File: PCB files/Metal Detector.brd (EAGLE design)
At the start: 100 x 80 mm, 121 parts, among them IC1 NE5534AD, IC2 BQ24133RGYR, IC3 LM317MBSTT3, IC4 ESP32-WROOM-32UE-N4, IC5 CP2102, IC6 LM317MBSTT3, J1 L-KLS1-TSJ3.5-013, J2/BATTERY DG128-5.0-02P-14, Q1 IRF740, Q2 BC556, Q3 SI2312CDS-T1-GE3, Q4 MBT3904DW1T1, Q5 SI2312CDS-T1-GE3, Q6 SI2323CDS-T1-GE3, T1 BC547, X1 A1944-50, X2 DC21MMX

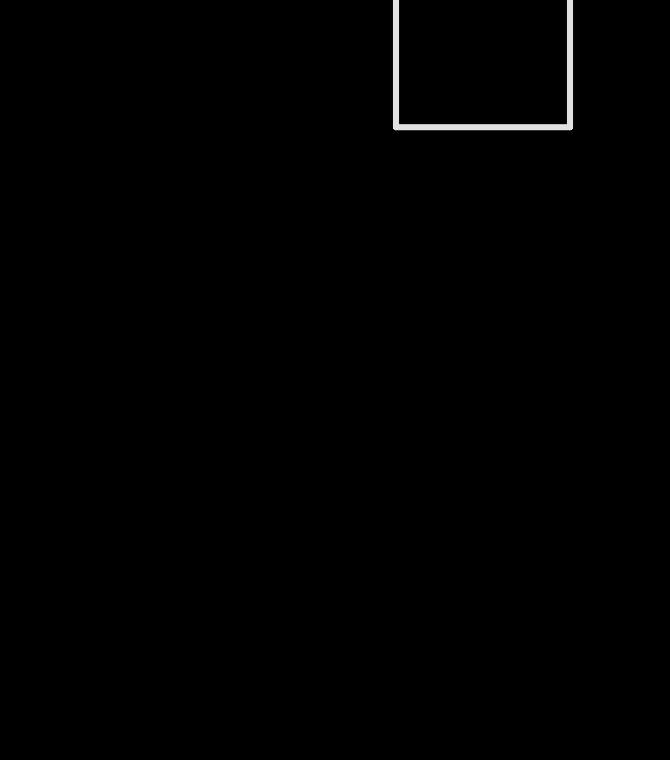
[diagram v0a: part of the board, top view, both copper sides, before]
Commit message: Add files via upload
adding speaker's control circuit (Design process still in progress)
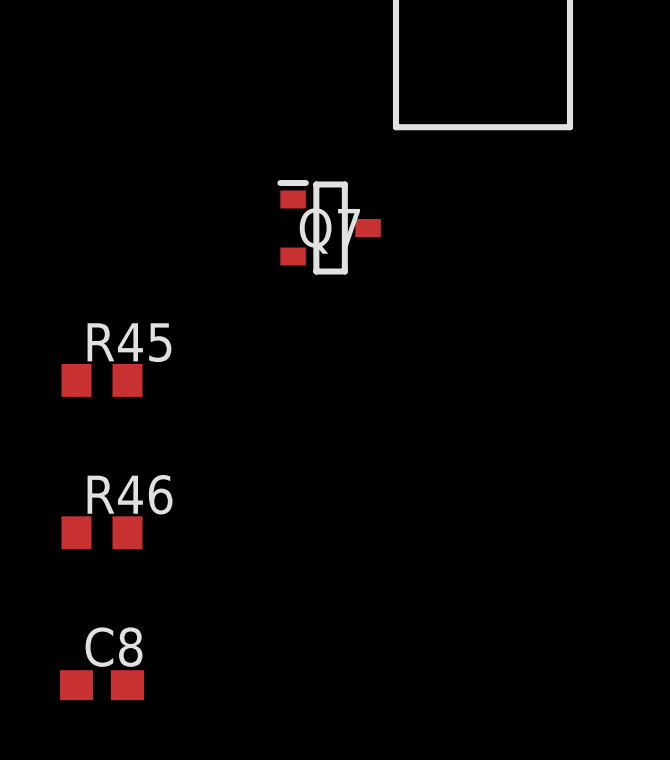
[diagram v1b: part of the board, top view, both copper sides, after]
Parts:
- added C8: 100nF, rcl:C0603
- added Q7: BC847AE6327HTSA1, BC847AE6327HTSA1:SOT95P240X110-3N
- added R45: 1KΩ, rcl:R0603
- added R46: 150Ω, rcl:R0603
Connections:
- new net N$26: LS1.2, Q7.3
- new net N$29: Q7.1, R45.1
- new net N$30: C8.2, LS1.1, R46.2
- new net N$31: R45.2
- net GND: now also Q7.2
- net VCC: now also C8.1, R46.1
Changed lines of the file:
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@@
 <attribute name="VALUE" x="-145.04" y="-559.55" size="1.27" layer="27" rot="R90"/>
+</element>
+<element name="Q7" library="BC847AE6327HTSA1" package="SOT95P240X110-3N" value="BC847AE6327HTSA1" x="-160.02" y="-608.33" smashed="yes">
+<attribute name="ARROW_PART_NUMBER" value="BC847AE6327HTSA1" x="-160.02" y="-608.33" size="1.778" layer="27" display="off"/>
+<attribute name="ARROW_PRICE-STOCK" value="https://www.arrow.com/en/products/bc847ae6327htsa1/infineon-technologies-ag?region=nac" x="-160.02" y="-608.33" size="1.778" layer="27" display="off"/>
+<attribute name="DESCRIPTION" value="TRANS NPN 45V 0.1A SOT-23" x="-160.02" y="-608.33" size="1.778" layer="27" display="off"/>
+<attribute name="HEIGHT" value="1.1mm" x="-160.02" y="-608.33" size="1.778" layer="27" display="off"/>
+<attribute name="MANUFACTURER_NAME" value="Infineon" x="-160.02" y="-608.33" size="1.778" layer="27" display="off"/>
+<attribute name="MANUFACTURER_PART_NUMBER" value="BC847AE6327HTSA1" x="-160.02" y="-608.33" size="1.778" layer="27" display="off"/>
+<attribute name="MOUSER_PART_NUMBER" value="726-BC847AE6327HTSA1" x="-160.02" y="-608.33" size="1.778" layer="27" display="off"/>
+<attribute name="MOUSER_PRICE-STOCK" value="https://www.mouser.co.uk/ProductDetail/Infineon-Technologies/BC847AE6327HTSA1?qs=K00xGehIljsR0IXot1V2vQ%3D%3D" x="-160.02" y="-608.33" size="1.778" layer="27" display="off"/>
+<attribute name="NAME" x="-160.02" y="-608.33" size="1.27" layer="25" align="center"/>
+<attribute name="VALUE" x="-160.02" y="-608.33" size="1.27" layer="27" align="center"/>
+</element>
+<element name="R45" library="rcl" library_urn="urn:adsk.eagle:library:334" package="R0603" package3d_urn="urn:adsk.eagle:package:23555/3" value="1KΩ" x="-167.64" y="-613.41" smashed="yes">
+<attribute name="NAME" x="-168.275" y="-612.775" size="1.27" layer="25"/>
+<attribute name="POPULARITY" value="70" x="-167.64" y="-613.41" size="1.778" layer="27" display="off"/>
+<attribute name="SPICEPREFIX" value="R" x="-167.64" y="-613.41" size="1.778" layer="27" display="off"/>
+<attribute name="VALUE" x="-168.275" y="-615.315" size="1.27" layer="27"/>
+</element>
+<element name="R46" library="rcl" library_urn="urn:adsk.eagle:library:334" package="R0603" package3d_urn="urn:adsk.eagle:package:23555/3" value="150Ω" x="-167.64" y="-618.49" smashed="yes">
+<attribute name="NAME" x="-168.275" y="-617.855" size="1.27" layer="25"/>
+<attribute name="POPULARITY" value="70" x="-167.64" y="-618.49" size="1.778" layer="27" display="off"/>
+<attribute name="SPICEPREFIX" value="R" x="-167.64" y="-618.49" size="1.778" layer="27" display="off"/>
+<attribute name="VALUE" x="-168.275" y="-620.395" size="1.27" layer="27"/>
+</element>
+<element name="C8" library="rcl" library_urn="urn:adsk.eagle:library:334" package="C0603" package3d_urn="urn:adsk.eagle:package:23616/2" value="100nF" x="-167.64" y="-623.57" smashed="yes">
+<attribute name="NAME" x="-168.275" y="-622.935" size="1.27" layer="25"/>
+<attribute name="POPULARITY" value="73" x="-167.64" y="-623.57" size="1.778" layer="27" display="off"/>
+<attribute name="SPICEPREFIX" value="C" x="-167.64" y="-623.57" size="1.778" layer="27" display="off"/>
+<attribute name="VALUE" x="-168.275" y="-625.475" size="1.27" layer="27"/>
 </element>
 </elements>
@@
 <contactref element="DS1" pad="2"/>
 <contactref element="R44" pad="1E"/>
+<contactref element="Q7" pad="2"/>
 <wire x1="-119.06" y1="-351.79" x2="-125.31" y2="-381" width="0" layer="19" extent="1-1"/>
 <wire x1="-123.9" y1="-335.28" x2="-119.06" y2="-351.79" width="0" layer="19" extent="1-1"/>
@@
 <wire x1="-141.39" y1="-598.17" x2="-138.43" y2="-593.09" width="0" layer="19" extent="1-1"/>
 <wire x1="-141.39" y1="-603.25" x2="-141.39" y2="-598.17" width="0" layer="19" extent="1-1"/>
+<wire x1="-161.27" y1="-609.28" x2="-141.39" y2="-603.25" width="0" layer="19" extent="1-1"/>
 <wire x1="-62.23" y1="-153.67" x2="-119.25" y2="-259.08" width="0" layer="19" extent="1-1"/>
 <wire x1="-16.51" y1="-153.67" x2="-62.23" y2="-153.67" width="0" layer="19" extent="1-1"/>
@@
 <contactref element="DS1" pad="19"/>
 <contactref element="R44" pad="1A"/>
+<contactref element="R46" pad="1"/>
+<contactref element="C8" pad="1"/>
 <wire x1="-143.09" y1="-598.17" x2="-143.09" y2="-603.25" width="0" layer="19" extent="1-1"/>
 <wire x1="-143.09" y1="-585.47" x2="-143.09" y2="-598.17" width="0" layer="19" extent="1-1"/>
+<wire x1="-168.49" y1="-618.49" x2="-143.09" y2="-603.25" width="0" layer="19" extent="1-1"/>
+<wire x1="-168.49" y1="-623.57" x2="-168.49" y2="-618.49" width="0" layer="19" extent="1-1"/>
 <wire x1="-159.94" y1="-553.57" x2="-143.09" y2="-585.47" width="0" layer="19" extent="1-1"/>
 <wire x1="-141.82" y1="-544.83" x2="-159.94" y2="-553.57" width="0" layer="19" extent="1-1"/>
@@
 <wire x1="-154.94" y1="-553.57" x2="-59.69" y2="-153.67" width="0" layer="19" extent="1-1"/>
 </signal>
+<signal name="N$26">
+<contactref element="LS1" pad="2"/>
+<contactref element="Q7" pad="3"/>
+<wire x1="-158.77" y1="-608.33" x2="-111.84" y2="-165.1" width="0" layer="19" extent="1-1"/>
+</signal>
+<signal name="N$29">
+<contactref element="R45" pad="1"/>
+<contactref element="Q7" pad="1"/>
+<wire x1="-161.27" y1="-607.38" x2="-168.49" y2="-613.41" width="0" layer="19" extent="1-1"/>
+</signal>
+<signal name="N$30">
+<contactref element="R46" pad="2"/>
+<contactref element="LS1" pad="1"/>
+<contactref element="C8" pad="2"/>
+<wire x1="-166.79" y1="-618.49" x2="-116.84" y2="-165.1" width="0" layer="19" extent="1-1"/>
+<wire x1="-166.79" y1="-623.57" x2="-166.79" y2="-618.49" width="0" layer="19" extent="1-1"/>
+</signal>
+<signal name="N$31">
+<contactref element="R45" pad="2"/>
+</signal>
 </signals>

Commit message: Add files via upload
Connected and added Spekers, volume and sensitivty connections with MCU
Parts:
- R45: value 1KΩ -> 1kΩ
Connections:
- net GND: now also R11.1E
- net IO32: now also R45.2
- net IO34: now also R12.1S
- net IO35: now also R11.1S
- net N$30: now also R12.1A; no longer LS1.1
- net N$31: now also LS1.1, R12.1E; no longer R45.2
- net VCC: now also R11.1A
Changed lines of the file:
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@@
 <attribute name="VALUE" x="-160.02" y="-608.33" size="1.27" layer="27" align="center"/>
 </element>
-<element name="R45" library="rcl" library_urn="urn:adsk.eagle:library:334" package="R0603" package3d_urn="urn:adsk.eagle:package:23555/3" value="1KΩ" x="-167.64" y="-613.41" smashed="yes">
+<element name="R45" library="rcl" library_urn="urn:adsk.eagle:library:334" package="R0603" package3d_urn="urn:adsk.eagle:package:23555/3" value="1kΩ" x="-167.64" y="-613.41" smashed="yes">
 <attribute name="NAME" x="-168.275" y="-612.775" size="1.27" layer="25"/>
 <attribute name="POPULARITY" value="70" x="-167.64" y="-613.41" size="1.778" layer="27" display="off"/>
@@
 <contactref element="R44" pad="1E"/>
 <contactref element="Q7" pad="2"/>
+<contactref element="R11" pad="1E"/>
 <wire x1="-119.06" y1="-351.79" x2="-125.31" y2="-381" width="0" layer="19" extent="1-1"/>
 <wire x1="-123.9" y1="-335.28" x2="-119.06" y2="-351.79" width="0" layer="19" extent="1-1"/>
@@
 <wire x1="-62.23" y1="-153.67" x2="-119.25" y2="-259.08" width="0" layer="19" extent="1-1"/>
 <wire x1="-16.51" y1="-153.67" x2="-62.23" y2="-153.67" width="0" layer="19" extent="1-1"/>
-<wire x1="-73.66" y1="-79.5528" x2="-62.23" y2="-153.67" width="0" layer="19" extent="1-1"/>
+<wire x1="-85.17" y1="-105.26" x2="-62.23" y2="-153.67" width="0" layer="19" extent="1-1"/>
+<wire x1="-73.66" y1="-79.5528" x2="-85.17" y2="-105.26" width="0" layer="19" extent="1-1"/>
 <wire x1="-68.6562" y1="-76.5556" x2="-73.66" y2="-79.5528" width="0" layer="19" extent="1-1"/>
 <wire x1="-69.85" y1="-64.77" x2="-68.6562" y2="-76.5556" width="0" layer="19" extent="1-1"/>
@@
 <contactref element="R46" pad="1"/>
 <contactref element="C8" pad="1"/>
+<contactref element="R11" pad="1A"/>
 <wire x1="-143.09" y1="-598.17" x2="-143.09" y2="-603.25" width="0" layer="19" extent="1-1"/>
 <wire x1="-143.09" y1="-585.47" x2="-143.09" y2="-598.17" width="0" layer="19" extent="1-1"/>
@@
 <wire x1="-64.77" y1="-153.67" x2="-116.13" y2="-274.32" width="0" layer="19" extent="1-1"/>
 <wire x1="-19.05" y1="-153.67" x2="-64.77" y2="-153.67" width="0" layer="19" extent="1-1"/>
-<wire x1="-67.125" y1="-65.52" x2="-64.77" y2="-153.67" width="0" layer="19" extent="1-1"/>
+<wire x1="-95.17" y1="-105.26" x2="-64.77" y2="-153.67" width="0" layer="19" extent="1-1"/>
+<wire x1="-67.125" y1="-65.52" x2="-95.17" y2="-105.26" width="0" layer="19" extent="1-1"/>
 <wire x1="-64.64" y1="-55.88" x2="-67.125" y2="-65.52" width="0" layer="19" extent="1-1"/>
 <wire x1="-63.92" y1="-50.8" x2="-64.64" y2="-55.88" width="0" layer="19" extent="1-1"/>
@@
 <signal name="IO34">
 <contactref element="IC4" pad="6"/>
+<contactref element="R12" pad="1S"/>
+<wire x1="-72.25" y1="-19.53" x2="-111.76" y2="-105.26" width="0" layer="19" extent="1-1"/>
 </signal>
 <signal name="IO35">
 <contactref element="IC4" pad="7"/>
+<contactref element="R11" pad="1S"/>
+<wire x1="-72.25" y1="-20.8" x2="-90.17" y2="-105.26" width="0" layer="19" extent="1-1"/>
 </signal>
 <signal name="IO32">
 <contactref element="IC4" pad="8"/>
+<contactref element="R45" pad="2"/>
+<wire x1="-166.79" y1="-613.41" x2="-72.25" y2="-22.07" width="0" layer="19" extent="1-1"/>
 </signal>
 <signal name="IO33">
@@
 <signal name="N$30">
 <contactref element="R46" pad="2"/>
+<contactref element="C8" pad="2"/>
+<contactref element="R12" pad="1A"/>
+<wire x1="-166.79" y1="-618.49" x2="-116.76" y2="-105.26" width="0" layer="19" extent="1-1"/>
+<wire x1="-166.79" y1="-623.57" x2="-166.79" y2="-618.49" width="0" layer="19" extent="1-1"/>
+</signal>
+<signal name="N$31">
+<contactref element="R12" pad="1E"/>
 <contactref element="LS1" pad="1"/>
-<contactref element="C8" pad="2"/>
-<wire x1="-166.79" y1="-618.49" x2="-116.84" y2="-165.1" width="0" layer="19" extent="1-1"/>
-<wire x1="-166.79" y1="-623.57" x2="-166.79" y2="-618.49" width="0" layer="19" extent="1-1"/>
-</signal>
-<signal name="N$31">
-<contactref element="R45" pad="2"/>
+<wire x1="-116.84" y1="-165.1" x2="-106.76" y2="-105.26" width="0" layer="19" extent="1-1"/>
 </signal>
 </signals>

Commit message: Add files via upload
Redesigned signal processing circuit due to ground layer
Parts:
- removed C4: 15pF, SparkFun-Capacitors:0402
- removed C5: 0.1uF, SparkFun-Capacitors:0402
- removed R6: 100kΩ, rcl:0207/10
- removed T1: BC547, transistor:TO92
- removed X1: A1944-50, con-coax:A1944
- added C12: 0.1uF, rcl:C0603
- added J2: DG128-7.5, DG128-7.5-02P-14-00AH:DG1287502P1400AH
- C1: value 50F -> 15pF; device Wurth_Capacitors_WCAP-STSC:WCAP-STSC_D18L40 -> rcl:C0603
- C2: device SparkFun-Capacitors:0402 -> rcl:C0603
- C3: value 0.1uF -> 2200uF; device SparkFun-Capacitors:0402 -> 2200uF capacitor:CAP_12.5_X_20_PAN
- D1: value BYV28-200 -> BYV28
- Q2: value BC556 -> BC847AE6327HTSA1; device transistor-pnp:TO92-EBC -> BC847AE6327HTSA1:SOT95P240X110-3N
- R1: value 10KΩ -> 20Ω
- R10: value 1KΩ -> 22kΩ; device rcl:0207/10 -> rcl:R1206
- R2: value 1RΩ -> 1mΩ; device rcl:0207/10 -> rcl:R1206
- R3: value 2k2Ω -> 10kΩ
- R4: value 4k7Ω -> 10kΩ
- R5: value 4k7 -> 6.8kΩ; device rcl:0207/10 -> rcl:R1206
- R7: value 10kΩ -> 1Ω
- R8: value 22KΩ -> 10kΩ
- R9: value 1MΩ -> 1kΩ; device rcl:0207/10 -> rcl:R1206
- moved C3 859.2 mm to (-171.4, -770.9)
- moved R8 794.0 mm to (-167.6, -711.2)
- moved C2 787.4 mm to (-172.7, -697.2)
- moved R10 783.1 mm to (-171.4, -703.6)
- moved D1 774.4 mm to (-166.4, -717.5)
- moved R9 767.5 mm to (-171.4, -685.8)
- moved R2 760.9 mm to (-171.4, -679.5)
- moved R7 760.2 mm to (-167.6, -674.4)
- moved R5 735.4 mm to (-171.4, -660.4)
- moved R4 721.8 mm to (-167.6, -645.2)
- moved C1 720.3 mm to (-172.7, -692.1)
- moved R3 719.1 mm to (-167.6, -640.1)
- moved R1 704.5 mm to (-167.6, -635.0)
- moved Q2 684.7 mm to (-165.1, -628.6)
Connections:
- removed net N$6 (its old number): R4.1, R5.2, T1.2
- removed net N$8: Q2.B, R6.2, R7.2
- new net N$32: D2.A, D3.C, TR1.2
- new net N$4: D1.A, R7.1
- net ADC_PIN: now also R2.2; no longer R9.2
- net GND: now also C1.2, C12.2, IC1.4, Q1.S, Q2.2, R9.1; no longer C1.1, C2.2, C4.1, D2.A, D3.C, R10.1, R6.1, TR1.2, X1.2, X1.3, X1.4, X1.5
- net N$1: now also D2.C, D3.A, IC1.3, R8.1; no longer R1.1, R2.2, TR1.1, X1.1
- net N$10: now also R10.1; no longer R8.1
- net N$11: now also C2.2; no longer C5.2
- net N$12: now also C1.1, R2.1, R9.2; no longer C4.2, R10.2, R9.1
- net N$13: now also C2.1; no longer C5.1
- net N$2: now also Q1.G; no longer D2.C, D3.A, IC1.3
- net N$3: now also Q2.3, R1.1, R3.1, R5.2; no longer D1.A, R2.1
- net N$5: now also Q2.1, R4.1; no longer Q1.G, R3.1, T1.3
- net N$7: now also J2.1, R7.2, R8.2, TR1.1; no longer Q2.C, R4.2
- net PULSE_PIN: now also R4.2; no longer R7.1
- net VCC: now also C12.1, J2.2, R10.2; no longer C1.2, C2.1, IC1.4, Q1.S, Q2.E, R8.2, T1.1

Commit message: Add files via upload
Fixed sum bug
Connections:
- removed net N$32: D2.A, D3.C, TR1.2
- net GND: now also D2.A, D3.C, TR1.2
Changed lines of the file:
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@@
 <contactref element="R9" pad="1"/>
 <contactref element="C3" pad="2"/>
+<contactref element="TR1" pad="2"/>
+<contactref element="D3" pad="C"/>
+<contactref element="D2" pad="A"/>
 <wire x1="-119.06" y1="-351.79" x2="-125.31" y2="-381" width="0" layer="19" extent="1-1"/>
 <wire x1="-123.9" y1="-335.28" x2="-119.06" y2="-351.79" width="0" layer="19" extent="1-1"/>
@@
 <wire x1="-41.72" y1="-13.47" x2="-44.265" y2="-19.08" width="0" layer="19" extent="1-1"/>
 <wire x1="-24.765" y1="26.61" x2="-41.72" y2="-13.47" width="0" layer="19" extent="1-1"/>
-<wire x1="-54.61" y1="30.48" x2="-24.765" y2="26.61" width="0" layer="19" extent="1-1"/>
-<wire x1="-44.95" y1="76.2" x2="-54.61" y2="30.48" width="0" layer="19" extent="1-1"/>
+<wire x1="-36.83" y1="30.48" x2="-24.765" y2="26.61" width="0" layer="19" extent="1-1"/>
+<wire x1="-44.45" y1="41.91" x2="-36.83" y2="30.48" width="0" layer="19" extent="1-1"/>
+<wire x1="-54.61" y1="30.48" x2="-44.45" y2="41.91" width="0" layer="19" extent="1-1"/>
+<wire x1="-68.58" y1="41.91" x2="-54.61" y2="30.48" width="0" layer="19" extent="1-1"/>
+<wire x1="-44.95" y1="76.2" x2="-44.45" y2="41.91" width="0" layer="19" extent="1-1"/>
 </signal>
 <signal name="VCC">
@@
 <wire x1="-116.84" y1="-165.1" x2="-106.76" y2="-105.26" width="0" layer="19" extent="1-1"/>
 </signal>
-<signal name="N$32">
-<contactref element="TR1" pad="2"/>
-<contactref element="D2" pad="A"/>
-<contactref element="D3" pad="C"/>
-<wire x1="-44.45" y1="41.91" x2="-68.58" y2="41.91" width="0" layer="19" extent="1-1"/>
-<wire x1="-36.83" y1="30.48" x2="-44.45" y2="41.91" width="0" layer="19" extent="1-1"/>
-</signal>
 <signal name="N$3">

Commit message: Add files via upload
Redesigned Regulators Circuit and editing sheet
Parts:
- removed C10, C13: 1uF, resistor:085CS_1AR
- removed C11, C14: 10uF, resistor:085CS_1AR
- removed C39, C40: 0.1uF, rcl:C2012
- removed D10, D11, D6, D7: 1N4002, diode:DO41-10
- removed FRAME3: FRAME-LEDGER, SparkFun-Aesthetics:CREATIVE_COMMONS
- removed IC3, IC6: LM317MBSTT3, v-reg:SOT223
- removed J1: L-KLS1-TSJ3.5-013, L-KLS1-TSJ3.5-013:LKLS1TSJ35013
- removed R14, R24: 240Ω, rcl:R0805
- removed R16: 394Ω, rcl:R0805
- removed R25: 720Ω, rcl:R0805
- added C4, C5: 47uF, rcl:SMC_A
- added C41, C42: 10uF/25v, rcl:C1210
- added C43: (no value), rcl:PANASONIC_D
- added C44, C50: 0.047uF, rcl:C0603
- added C45: 4.7uF/10V, rcl:C0805
- added C46, C51: 47uF/6.3V, SparkFun-Capacitors:1206
- added C47, C48, C52, C53: 10uF/6.3V, rcl:C0805
- added C49, C54: 470pF, rcl:C0603
- added C55: 22nF, rcl:C0603
- added C57: 33nF, rcl:C0603
- added D14, D5: SS33-E3_57T, SS33-E3_57T:DIOM7959X262N
- added IC7: TPS54386PWPRG4, TPS54386PWPRG4:SOP65P640X120-15N
- added JP1: (no value), pinhead:1X03
- added L2, L4: SRP7028AA-8R2M, SRP7028AA-8R2M:INDPM7166X300N
- added R47, R6: 1KΩ, rcl:R0603
- added R48, R49: 10Ω, rcl:R0603
- added R50, R51: 20.5kΩ, rcl:R0603
- added R52: 3.32kΩ, rcl:R0603
- added R53: 6.49kΩ, rcl:R0603
- added R55: 1.54kΩ, rcl:R0603
- added R56: 3.83kΩ, rcl:R0603
- R4: value 10kΩ -> 2.2kΩ
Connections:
- removed net ADC_PIN: IC1.6, R2.2
- removed net N$15: C11.+, D7.A, IC3.1, R24.1, R25.2
- removed net N$20: C14.+, D11.A, IC6.1, R14.1, R16.2
- removed net PULSE_PIN: R4.2
- new net FB1: C57.1, IC7.7, R51.2, R56.1
- new net FB2: C55.1, IC7.8, R50.2, R53.1
- new net N$32: C5.+, R47.1
- new net N$33: C4.-, JP1.1
- new net N$34: C5.-, JP1.2
- new net N$35: C44.2, IC7.13
- new net N$36: C44.1, C49.1, D5.1, IC7.12, L2.1
- new net N$37: C45.2, IC7.11, IC7.9
- new net N$38: C55.2, R52.1
- new net N$39: C50.2, IC7.2
- new net N$40: C49.2, R48.1
- new net N$41: C57.2, R55.1
- new net N$42: C50.1, C54.1, D14.1, IC7.3, L4.1
- new net N$44: C54.2, R49.1
- new net N$8: C4.+, R6.1
- new net VCCIO: C46.1, C47.2, C48.2, DS1.19, L2.2, R11.1A, R17.2, R18.2, R50.1
- new net VCCIO1: C51.1, C52.2, C53.2, L4.2, R51.1
- net GND: now also C41.2, C42.2, C43.-, C45.1, C46.2, C47.1, C48.1, C51.2, C52.1, C53.1, D14.2, D5.2, IC7.15, IC7.4, IC7.5, IC7.6, JP1.3, R48.2, R49.2, R52.2, R53.2, R55.2, R56.2; no longer C10.-, C11.-, C13.-, C14.-, C39.2, C40.2, R16.1, R25.1
- net IO18: now also R4.2
- net IO25: now also R6.2
- net IO26: now also R47.2
- net IO4: now also IC1.6, R2.2
- net VCC: now also C41.1, C42.1, C43.+, IC7.1, IC7.14; no longer C10.+, C13.+, C39.1, C40.1, D10.A, D10.C, D11.C, D6.A, D6.C, D7.C, DS1.19, IC3.3, IC3.4, IC6.3, IC6.4, R11.1A, R14.2, R17.2, R18.2, R24.2

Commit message: Add files via upload
Redesigned Uaer Interface Block for Encoder (Encoder will include other design step)
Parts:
- removed R11, R12, R44: PC16S, piher:PC16S
- removed R46: 150Ω, rcl:R0603
- added IC3: MCP4017T-503E_LT, MCP4017T-503E_LT:SOT65P210X110-6N
- added Q8: BC847AE6327HTSA1, BC847AE6327HTSA1:SOT95P240X110-3N
- added S1: (no value), switch:MS243
- C43: value (none) -> 100uF
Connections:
- removed net N$31: LS1.1, R12.1E
- new net N$15: DS1.3, Q8.2
- new net N$20: IC3.5, LS1.1
- new net V_SYS_IN: C28.1, C35.1, Q6.2, R30.2, R31.2, S1.1
- net GND: now also C8.2, IC3.2; no longer R11.1E, R44.1E
- net IO18: no longer R4.2
- net IO19: now also R4.2
- net IO33: now also Q8.1
- net IO34: no longer R12.1S
- net IO35: no longer R11.1S
- net N$28: now also IC3.3; no longer DS1.3, R44.1S
- net N$30: now also IC3.4; no longer C8.2, R12.1A, R46.2
- net PVCC: no longer C28.1, C35.1, Q6.2, R30.2, R31.2
- net VCC: now also IC3.1, IC3.6, Q8.3, S1.2; no longer R44.1A, R46.1
- net VCCIO: no longer R11.1A

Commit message: Add files via upload
Add connector to User Interface
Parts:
- removed DS1: WG12864B-TFH-V#N, NHD-12864WG-BTGH-T#N:NHD12864WGBTGHTN
- removed J2/BATTERY: DG128-5.0-02P-14, DG128-5.0-02P-14:DG1285002P14
- removed JP1: (no value), pinhead:1X03
- removed LS1: MCKPT-G1340-3917, MCKPT-G1340-3917:MCKPTG13403917
- removed S1: (no value), switch:MS243
- removed U$1: 103AP-2, 130-AP2:AT-2_SMI
- added J1: DG128-7.5, DG128-7.5-02P-14-00AH:DG1287502P1400AH
- added J3: DG129-5.0-03P-14-00AH, DG129-5.0-03P-14-00AH:CONN3_DG129-5.0-03P-14-00AH_DE
- added R11: 1kΩ, rcl:R0603
- added R12: 560Ω, rcl:R0603
- added X1: 22-23-2031, con-molex:22-23-2031
- added X3: 22-23-2051, con-molex:22-23-2051
- added X4: 22-23-2021, con-molex:22-23-2021
- added X5: 22-23-2091, con-molex:22-23-2091
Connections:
- removed net N$24: C31.1, C32.1, C33.1, J2/BATTERY.1, Q6.3, R33.2, R34.2
- removed net N$28: IC3.3
- removed net N$30: IC3.4
- removed net STAT: IC2.9
- new net N$31: Q8.1, R11.1
- net GND: now also J3.2, X1.3, X3.5, X5.2, X5.9; no longer DS1.2, DS1.20, J2/BATTERY.2, JP1.3, U$1.2
- net IO18: now also X5.7; no longer DS1.17
- net IO19: now also X5.4
- net IO21: now also IC3.4
- net IO22: now also IC3.3; no longer DS1.14
- net IO23: now also X5.5; no longer DS1.15
- net IO33: now also R11.2; no longer Q8.1
- net IO34: now also X3.3
- net IO35: now also IC2.9
- net IO4: now also R12.1, R12.2
- net IO5: now also X5.6; no longer DS1.16
- net N$15: now also X5.3; no longer DS1.3
- net N$20: now also X4.1; no longer LS1.1
- net N$26: now also X4.2; no longer LS1.2
- net N$33: now also X1.1; no longer JP1.1
- net N$34: now also X1.2; no longer JP1.2
- net SENSOR_VN: now also X3.2
- net SENSOR_VP: now also X3.1
- net TS: now also J3.3; no longer U$1.1
- net VBATT: now also C31.1, C32.1, C33.1, J3.1, Q6.3, R33.2, R34.2
- net VCC: now also J1.1, X3.4, X5.1; no longer DS1.1, S1.2
- net VCCIO: now also X5.8; no longer DS1.19
- net V_SYS_IN: now also J1.2; no longer S1.1
